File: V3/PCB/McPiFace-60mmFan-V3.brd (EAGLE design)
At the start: 88 x 88 mm, 30 parts, among them J2 Fan, J5 Programming Interface, Q1 4.3A/20V/54mΩ, Q2 220mA/50V/3.5Ω, U1 Tiny85-20-SMT, U3 LIS3DH

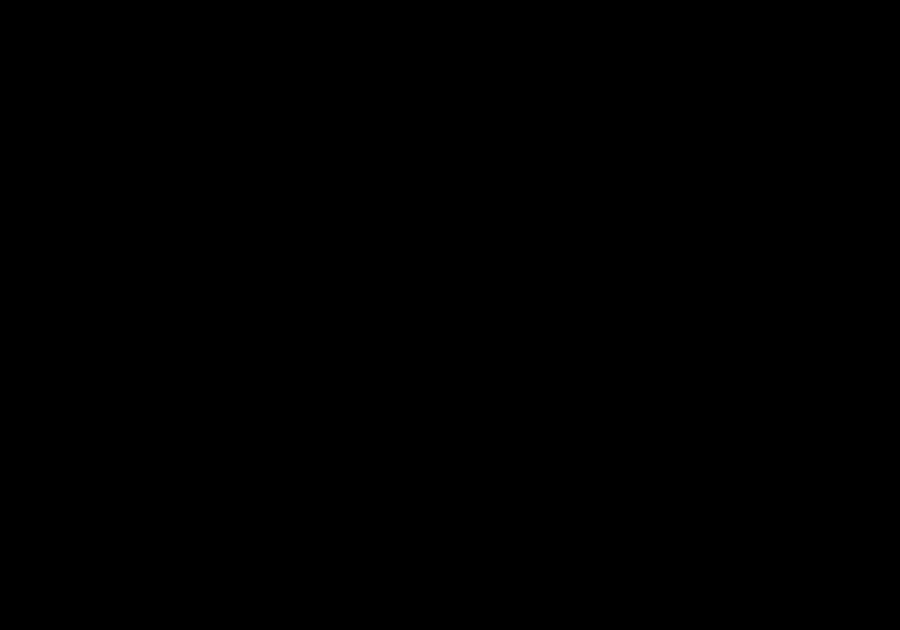
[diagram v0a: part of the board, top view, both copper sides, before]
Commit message: Modified V3 to include some package details.
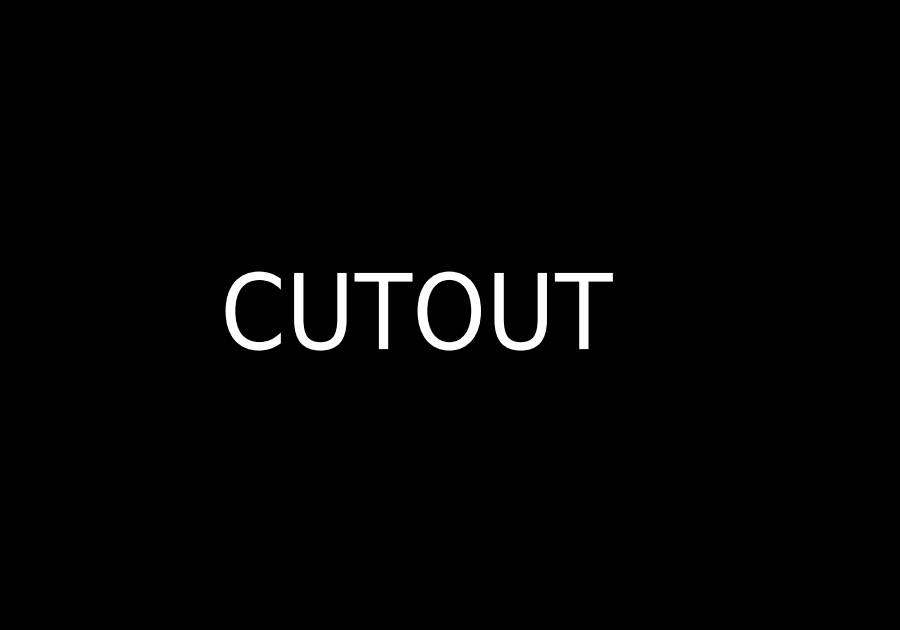
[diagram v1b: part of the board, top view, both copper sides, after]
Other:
- board text added: "CUTOUT"
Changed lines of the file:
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@@
 <text x="61.2" y="5.5" size="1.778" layer="26" ratio="15" rot="MR0">S.Harrison 16 Jan 2019</text>
 <text x="59" y="81.3" size="2.1844" layer="26" ratio="15" rot="MR0">ThingySticks.com</text>
+<text x="38.2" y="49.5" size="2.54" layer="20">CUTOUT</text>
 </plain>
 <attributes>
